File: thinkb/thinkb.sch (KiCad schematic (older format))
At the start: 149 parts, among them P1 battery+, P2 battery-, SW1 SW_Push, SW11 SW_Push, SW12 SW_Push, SW13 SW_Push, SW14 SW_Push, SW15 SW_Push, SW16 SW_Push, SW17 SW_Push, SW18 SW_Push, SW19 SW_Push, SW2 SW_Push, SW20 SW_Push, SW21 SW_Push, SW22 SW_Push, SW23 SW_Push, SW24 SW_Push, SW25 SW_Push, SW26 SW_Push, SW27 SW_Push, SW28 SW_Push, SW29 SW_Push, SW3 SW_Push, SW30 SW_Push, SW31 SW_Push, SW32 SW_Push, SW33 SW_Push, SW34 SW_Push, SW35 SW_Push, SW36 SW_Push, SW37 SW_Push, SW38 SW_Push, SW39 SW_Push, SW4 SW_Push, SW40 SW_Push, SW41 SW_Push, SW42 SW_Push, SW43 SW_Push, SW44 SW_Push, SW45 SW_Push, SW46 SW_Push, SW47 SW_Push, SW48 SW_Push, SW49 SW_Push, SW5 SW_Push, SW50 SW_Push, SW51 SW_Push, SW52 SW_Push, SW53 SW_Push, SW54 SW_Push, SW55 SW_Push, SW56 SW_Push, SW57 SW_Push, SW58 SW_Push, SW59 SW_Push, SW6 SW_Push, SW60 SW_Push, SW61 SW_Push, SW62 Reset, SW63 Power, SW7 SW_Push, SW8 SW_Push, SW9 SW_Push

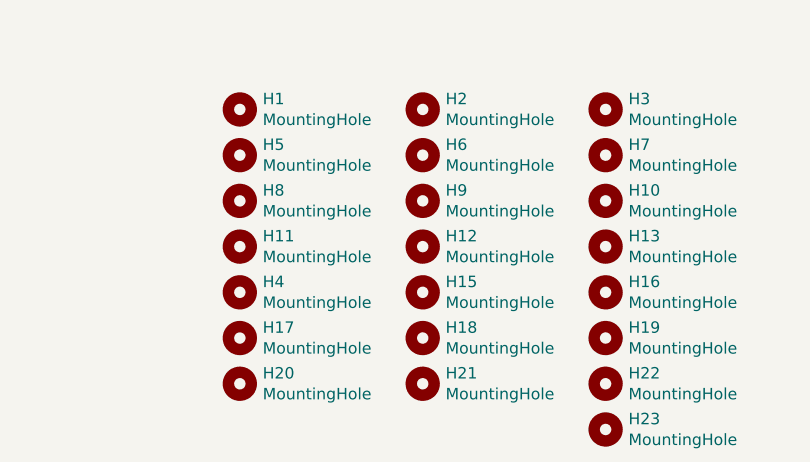
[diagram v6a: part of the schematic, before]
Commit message: Removed extra holes
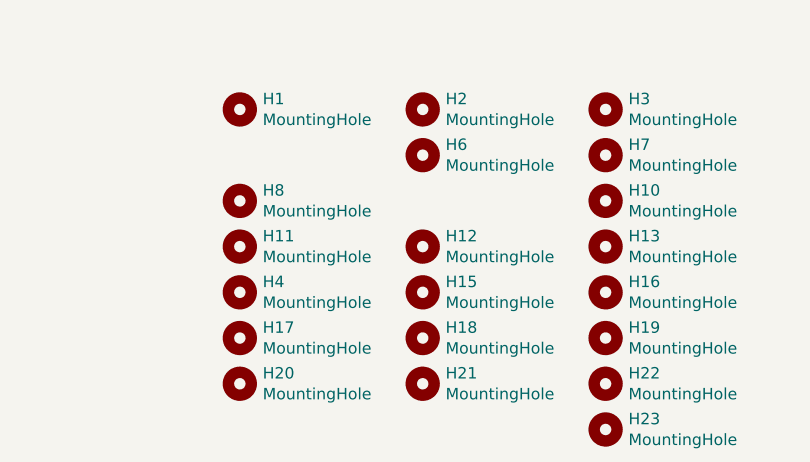
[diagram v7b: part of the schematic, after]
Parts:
- removed H5, H9: MountingHole, MountingHole:MountingHole_2.2mm_M2, symbol Mechanical:MountingHole
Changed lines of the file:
@@
-$EndComp
-$Comp
-L Mechanical:MountingHole H5
-U 1 1 61545B9C
-P 7600 1150
-F 0 "H5" H 7700 1196 50  0000 L CNN
-F 1 "MountingHole" H 7700 1105 50  0000 L CNN
-F 2 "MountingHole:MountingHole_2.2mm_M2" H 7600 1150 50  0001 C CNN
-F 3 "~" H 7600 1150 50  0001 C CNN
-	1    7600 1150
-	1    0    0    -1
 $EndComp
 $Comp
@@
 	1    0    0    -1
 $EndComp
-$Comp
-L Mechanical:MountingHole H9
-U 1 1 6158B5F0
-P 8400 1350
-F 0 "H9" H 8500 1396 50  0000 L CNN
-F 1 "MountingHole" H 8500 1305 50  0000 L CNN
-F 2 "MountingHole:MountingHole_2.2mm_M2" H 8400 1350 50  0001 C CNN
-F 3 "~" H 8400 1350 50  0001 C CNN
-	1    8400 1350
-	1    0    0    -1
-$EndComp

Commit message: Routing
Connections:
- net at P1.1 (Pin_1): now also SW63.3 (C); no longer SW63.1 (A)
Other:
- moved on the sheet: P1
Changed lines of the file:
@@
 L pin_pad:i2c_pin P1
 U 1 1 6151B959
-P 9750 3600
-F 0 "P1" H 9830 3642 50  0000 L CNN
-F 1 "battery+" H 9830 3551 50  0000 L CNN
-F 2 "footprints:1pin_conn" H 9750 3600 50  0001 C CNN
-F 3 "" H 9750 3600 50  0001 C CNN
-	1    9750 3600
+P 9750 3800
+F 0 "P1" H 9830 3842 50  0000 L CNN
+F 1 "battery+" H 9830 3751 50  0000 L CNN
+F 2 "footprints:1pin_conn" H 9750 3800 50  0001 C CNN
+F 3 "" H 9750 3800 50  0001 C CNN
+	1    9750 3800
 	1    0    0    -1
 $EndComp
@@
 Wire Wire Line
 	9150 3700 8600 3700
-NoConn ~ 9550 3800
+NoConn ~ 9550 3600
 Wire Wire Line
 	9550 4000 9150 4000
